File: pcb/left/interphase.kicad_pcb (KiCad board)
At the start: 2 copper layers, 138.1 x 95.2 mm, 69 parts, among them J1 Conn_01x04_Male, SW10 MOM-SPST, SW11 MOM-SPST, SW12 MOM-SPST, SW13 MOM-SPST, SW14 MOM-SPST, SW15 MOM-SPST, SW16 MOM-SPST, SW17 MOM-SPST, SW18 MOM-SPST, SW19 MOM-SPST, SW2 MOM-SPST, SW20 MOM-SPST, SW21 MOM-SPST, SW22 MOM-SPST, SW23 MOM-SPST, SW24 MOM-SPST, SW25 MOM-SPST, SW26 MOM-SPST, SW27 MOM-SPST, SW28 MOM-SPST, SW29 MOM-SPST, SW3 MOM-SPST, SW30 MOM-SPST, SW31 MOM-SPST, SW32 MOM-SPST, SW4 MOM-SPST, SW5 MOM-SPST, SW7 MOM-SPST, SW8 MOM-SPST, SW9 MOM-SPST, U1 Core51822B, U2 MCP1640

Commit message: change pcb
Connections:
- J1 pad 2: Net-(J1-Pad2) -> GND
- J1 pad 4: GND -> Net-(J1-Pad4)
- U1 pad 32: Net-(J1-Pad2) -> Net-(J1-Pad4)
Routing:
- net Net-(J1-Pad2): track 14.2 -> 0.00 mm, vias 2 -> 0
- net Net-(J1-Pad4): track 0.00 -> 10.9 mm
- net GND: track 105.5 -> 101.6 mm

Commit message: can send basic chars
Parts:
- removed C1: 4,7µF, Capacitors_SMD:C_0805_HandSoldering
- removed C2: 10µF, Capacitors_SMD:C_0805_HandSoldering
- removed L1: 4,7µH, SMD_Packages:SMD-1206_Pol
- removed R1: 536K, Resistors_SMD:R_0805
- removed R2: 309K, Resistors_SMD:R_0805
- removed U2: MCP1640, TO_SOT_Packages_SMD:SOT-23-6
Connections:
- BT1 pad 1: +BATT -> +3V3
- D21 pad 1: /col4 -> Net-(D21-Pad1)
- D22 pad 1: /col4 -> Net-(D21-Pad1)
- D23 pad 1: /col4 -> Net-(D21-Pad1)
- D24 pad 1: /col4 -> Net-(D21-Pad1)
- D25 pad 1: /col4 -> Net-(D21-Pad1)
- U1 pad 15: +BATT -> Net-(U1-Pad15)
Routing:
- net /col4: track 172.6 -> 0.85 mm
- net Net-(D21-Pad1): track 0.00 -> 88.4 mm
- net +BATT: track 60.6 -> 0.00 mm, vias 3 -> 0
- net GND: track 101.6 -> 82.6 mm
- net +3V3: track 49.9 -> 60.8 mm, vias 3 -> 0
- net Net-(L1-Pad2): track 8.19 -> 0.00 mm
- net Net-(R1-Pad2): track 5.44 -> 0.00 mm

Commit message: some changes
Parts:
- added SW1: SW_SPDT, Button_Switch_Keyboard:SW_E-Switch_EG1224_SPDT_Angled, F.Cu at (53.2, 76.4)
- moved J1 26.5 mm to (54.0, 80.6), turned to 270 degrees
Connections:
- BT1 pad 1: +3V3 -> Net-(BT1-Pad1)
- D21 pad 1: Net-(D21-Pad1) -> /col4
- D22 pad 1: Net-(D21-Pad1) -> /col4
- D23 pad 1: Net-(D21-Pad1) -> /col4
- D24 pad 1: Net-(D21-Pad1) -> /col4
- D25 pad 1: Net-(D21-Pad1) -> /col4
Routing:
- net /col4: track 0.85 -> 173.6 mm
- net Net-(D21-Pad1): track 88.4 -> 0.00 mm
- net Net-(J1-Pad4): track 10.9 -> 74.9 mm, vias 0 -> 3
- net Net-(J1-Pad3): track 13.2 -> 69.9 mm, vias 0 -> 3
- net +3V3: track 60.8 -> 23.5 mm
- net Net-(BT1-Pad1): track 0.00 -> 20.1 mm
- net Net-(D9-Pad2): track 7.62 -> 0.00 mm
- net /row4: track 118.0 -> 123.8 mm
- net /col0: track 98.5 -> 102.3 mm
- net GND: track 82.6 -> 85.5 mm

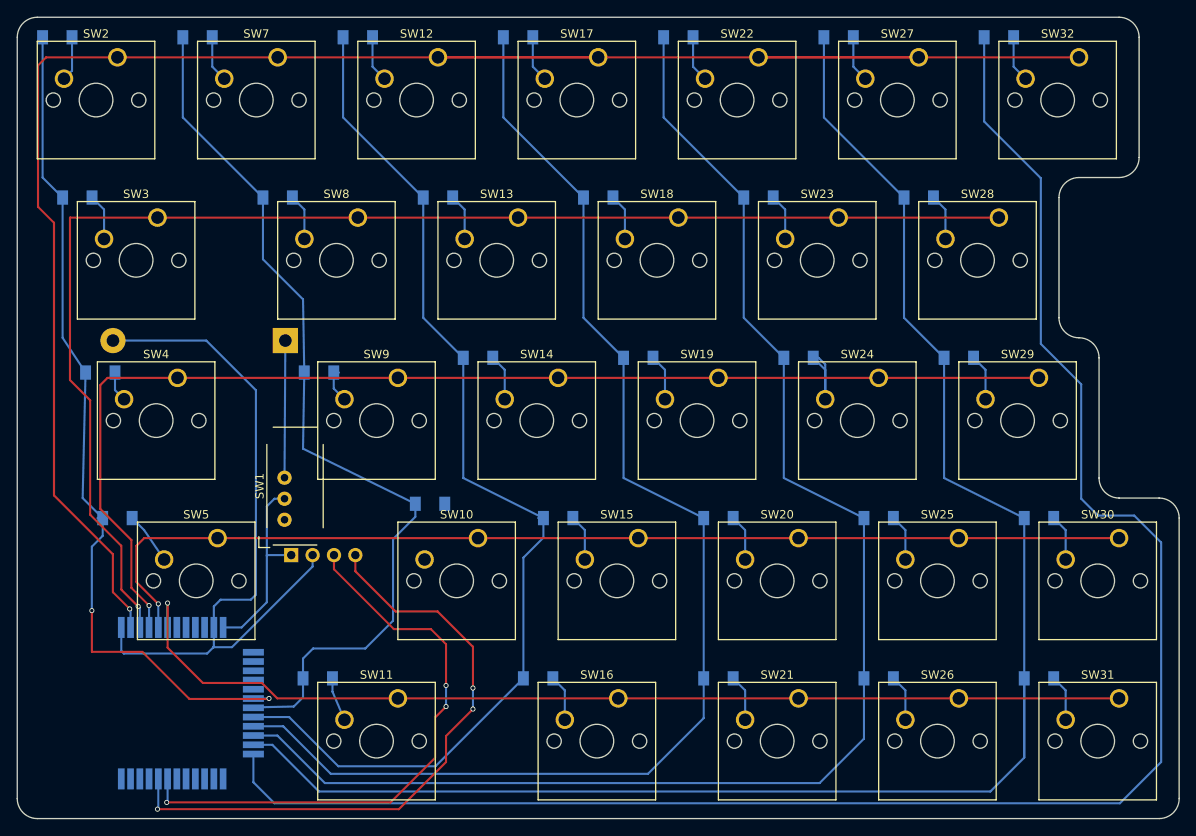
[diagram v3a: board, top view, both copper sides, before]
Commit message: change to actual matrix
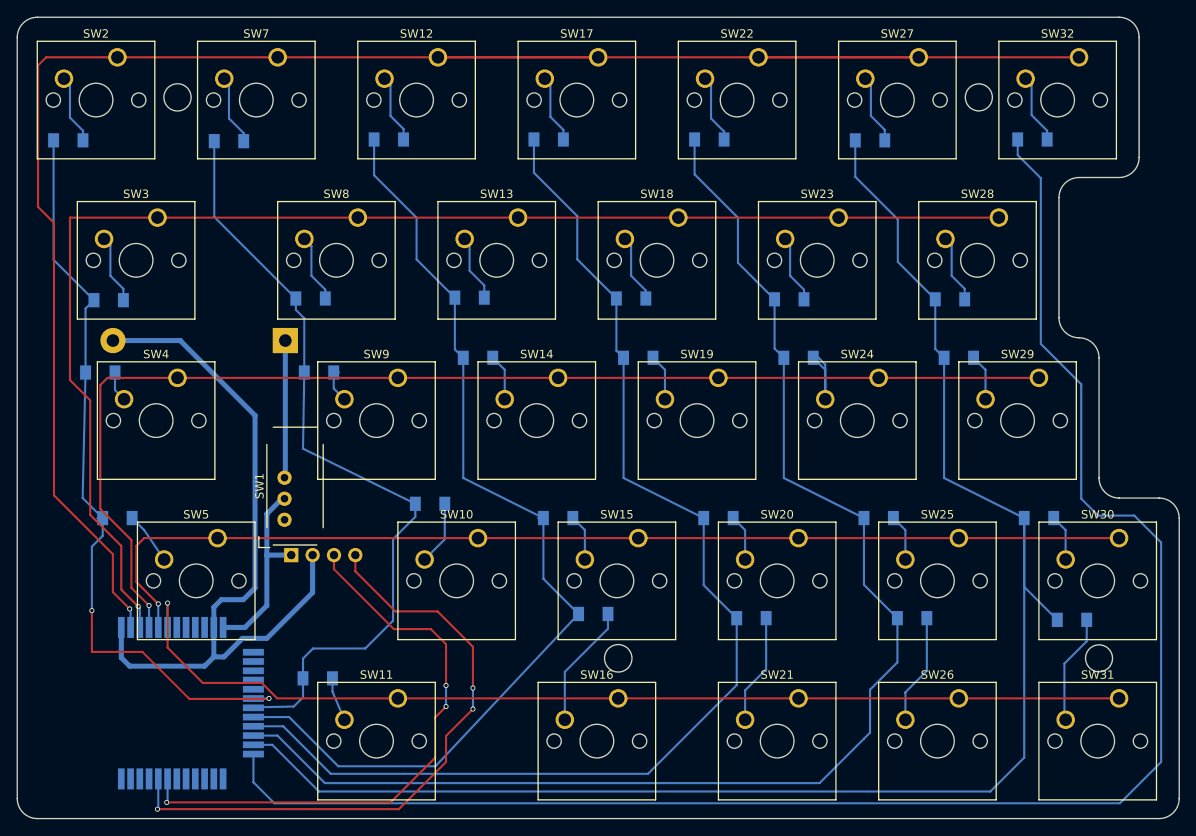
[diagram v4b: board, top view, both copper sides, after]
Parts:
- moved D6 12.9 mm to (46.6, 31.4)
- moved D26 12.8 mm to (122.8, 31.3)
- moved D31 12.8 mm to (142.1, 31.2)
- moved D2 12.8 mm to (32.3, 50.3)
- moved D21 12.7 mm to (103.7, 31.2)
- moved D11 12.7 mm to (65.6, 31.2)
- moved D16 12.7 mm to (84.6, 31.2)
- moved D27 12.7 mm to (132.3, 50.2)
- moved D22 12.6 mm to (113.2, 50.2)
- moved D17 12.6 mm to (94.4, 50.1)
- moved D7 12.6 mm to (56.3, 50.1)
- moved D12 12.5 mm to (75.2, 50.0)
- moved D1 12.3 mm to (27.5, 31.3)
- moved D15 10.1 mm to (89.9, 87.6)
- moved D25 8.18 mm to (127.8, 88.1)
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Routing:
- net /col1: track 108.2 -> 94.4 mm
- net /col6: track 211.7 -> 197.9 mm
- net /col0: track 102.3 -> 90.6 mm
- net /col2: track 128.5 -> 117.9 mm
- net /col3: track 151.3 -> 140.9 mm
- net /col4: track 173.6 -> 163.2 mm
- net /col5: track 202.7 -> 193.2 mm
- net Net-(D15-Pad2): track 5.51 -> 14.7 mm
- net Net-(D25-Pad2): track 5.51 -> 13.1 mm
- net Net-(D9-Pad2): track 0.00 -> 7.62 mm
- net Net-(D20-Pad2): track 5.51 -> 13.1 mm
- net Net-(D30-Pad2): track 5.51 -> 13.0 mm
- net Net-(D1-Pad2): track 5.32 -> 8.27 mm
- net Net-(D6-Pad2): track 5.51 -> 8.39 mm
- net Net-(D31-Pad2): track 5.51 -> 8.29 mm
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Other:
- outline, holes or cut-outs redrawn

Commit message: save previous work
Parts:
- added SW101: SW_SPDT, Button_Switch_Keyboard:SW_E-Switch_EG1224_SPDT_Angled, F.Cu at (46.8, 73.6)
- added SW102: SW_SPDT, Button_Switch_Keyboard:SW_E-Switch_EG1224_SPDT_Angled, F.Cu at (40.0, 74.9)
- added U2: Core51822B, Misc:Core51822(B), F.Cu at (38.6, 98.2)
- moved BT1 12.8 mm to (66.1, 54.2)
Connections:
- U1 pad 31: Net-(J1-Pad3) -> Net-(SW102-Pad1)
- U1 pad 32: Net-(J1-Pad4) -> Net-(SW101-Pad1)
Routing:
- net Net-(SW102-Pad1): track 0.00 -> 76.4 mm, vias 0 -> 1
- net Net-(SW101-Pad1): track 0.00 -> 75.2 mm, vias 0 -> 2
- net Net-(J1-Pad4): track 74.9 -> 25.8 mm, vias 3 -> 1
- net Net-(SW101-Pad3): track 0.00 -> 47.3 mm, vias 0 -> 2
- net Net-(SW102-Pad3): track 0.00 -> 46.1 mm, vias 0 -> 1
- net Net-(J1-Pad3): track 69.9 -> 43.8 mm, vias 3 -> 1
- net Net-(U1-Pad35): track 0.40 -> 23.8 mm, vias 0 -> 1
- net Net-(U1-Pad36): track 0.00 -> 20.6 mm, vias 0 -> 1
- net Net-(U1-Pad34): track 0.00 -> 20.4 mm, vias 0 -> 1
- net +3V3: track 23.4 -> 42.7 mm, vias 0 -> 1
- net Net-(U1-Pad33): track 0.00 -> 18.5 mm, vias 0 -> 1
- net GND: track 87.7 -> 105.7 mm, vias 0 -> 1
- net Net-(BT1-Pad1): track 20.3 -> 30.7 mm, vias 0 -> 1
- net /row4: track 123.8 -> 120.5 mm
- net Net-(D4-Pad2): track 6.25 -> 7.56 mm
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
